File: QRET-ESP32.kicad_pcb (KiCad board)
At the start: 2 copper layers, 9 parts, among them J1 Conn_01x04_Socket, J2 Conn_01x02_Socket, J3 Conn_01x02_Socket, J4 Conn_02x04_Counter_Clockwise, J5 Conn_01x02_Socket, J6 Conn_01x02_Socket, J7 Conn_01x02_Socket, U1 ESP32-S2-DevKitC-1, U2 ADS1115IDGS

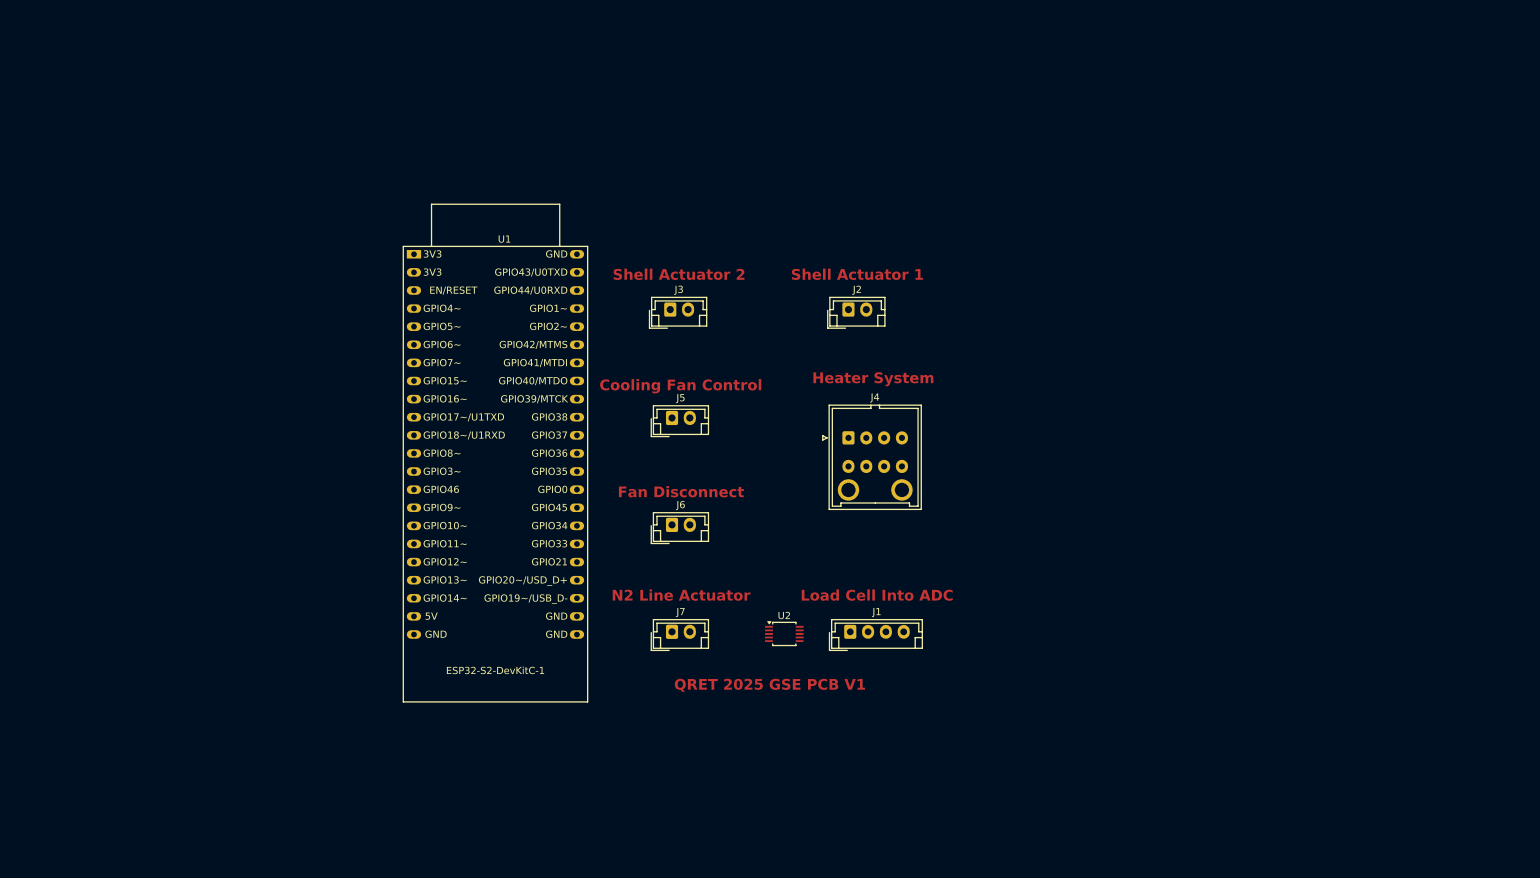
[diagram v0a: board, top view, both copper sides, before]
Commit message: Updated to 4-pin fans, moved power pages together, deleted old reference.
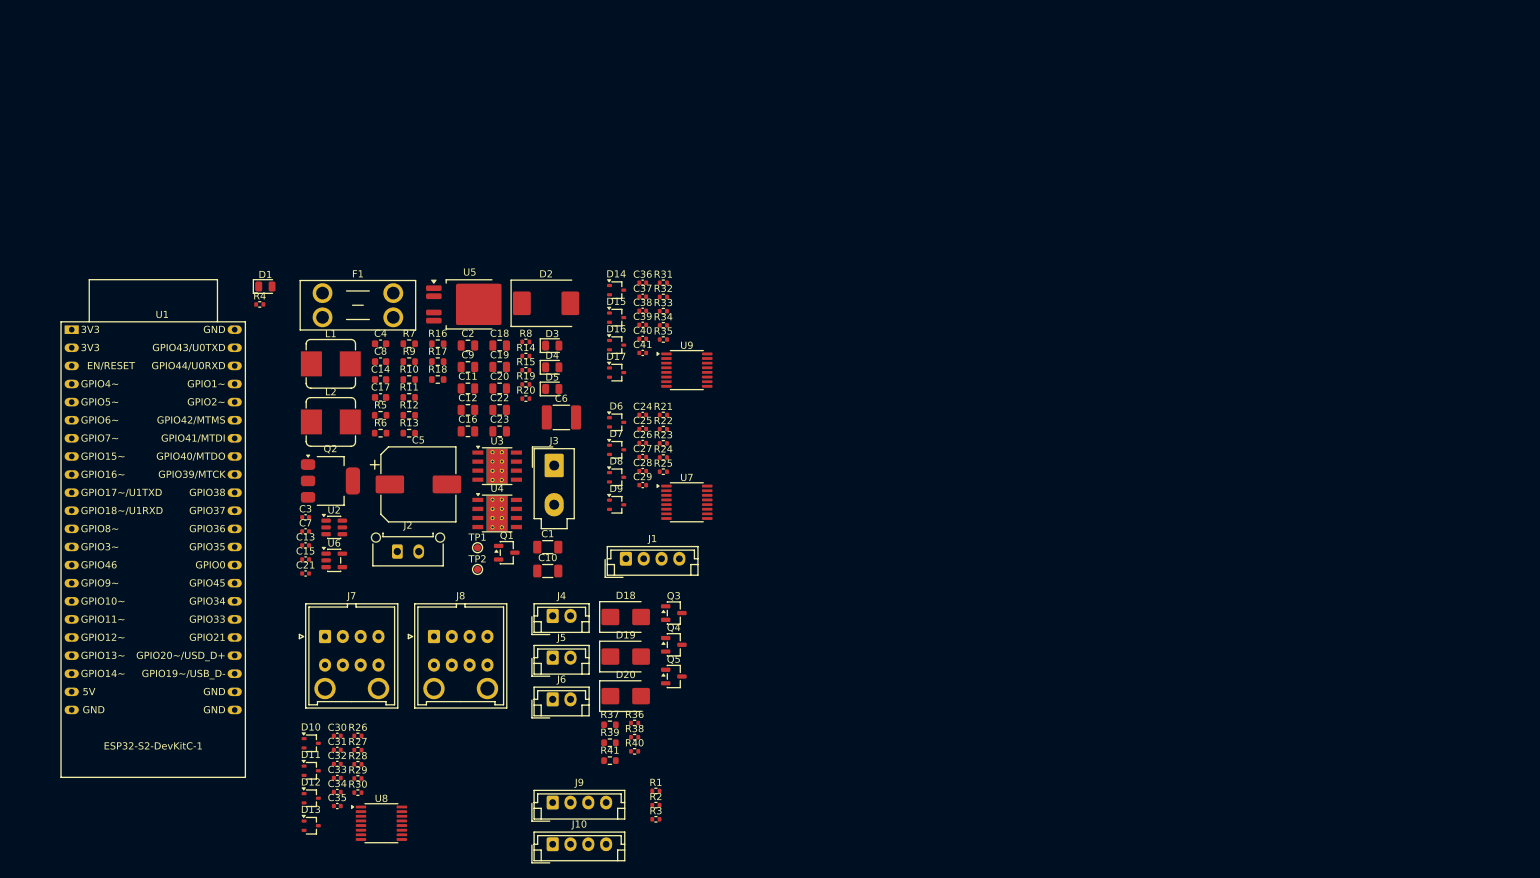
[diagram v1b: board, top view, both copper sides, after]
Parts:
- added C1: 10uF, Capacitor_SMD:C_1206_3216Metric, F.Cu at (140.8, 110.3)
- added C10: 10uF, Capacitor_SMD:C_1206_3216Metric, F.Cu at (140.8, 113.7)
- added C11: 22uF, Capacitor_SMD:C_0805_2012Metric, F.Cu at (129.6, 88.1)
- added C12: 220nF, Capacitor_SMD:C_0805_2012Metric, F.Cu at (129.6, 91.1)
- added C13: 0.1μF, Capacitor_SMD:C_0402_1005Metric, F.Cu at (106.8, 110.1)
- added C14: 1uF, Capacitor_SMD:C_0603_1608Metric, F.Cu at (117.4, 86.8)
- added C15: 0.1μF, Capacitor_SMD:C_0402_1005Metric, F.Cu at (106.8, 112.0)
- added C16: 10uF, Capacitor_SMD:C_0805_2012Metric, F.Cu at (129.6, 94.1)
- added C17: 3pF, Capacitor_SMD:C_0603_1608Metric, F.Cu at (117.4, 89.3)
- added C18: 22uF, Capacitor_SMD:C_0805_2012Metric, F.Cu at (134.1, 82.0)
- added C19: 22uF, Capacitor_SMD:C_0805_2012Metric, F.Cu at (134.1, 85.0)
- added C2: 220nF, Capacitor_SMD:C_0805_2012Metric, F.Cu at (129.6, 82.0)
- added C20: 10uF, Capacitor_SMD:C_0805_2012Metric, F.Cu at (134.1, 88.1)
- added C21: 0.1μF, Capacitor_SMD:C_0402_1005Metric, F.Cu at (106.8, 114.0)
- added C22: 10uF, Capacitor_SMD:C_0805_2012Metric, F.Cu at (134.1, 91.1)
- added C23: 10uF, Capacitor_SMD:C_0805_2012Metric, F.Cu at (134.1, 94.1)
- added C24: 0.1μF, Capacitor_SMD:C_0402_1005Metric, F.Cu at (154.1, 91.8)
- added C25: 0.1μF, Capacitor_SMD:C_0402_1005Metric, F.Cu at (154.1, 93.7)
- added C26: 150nF, Capacitor_SMD:C_0402_1005Metric, F.Cu at (154.1, 95.7)
- added C27: 150nF, Capacitor_SMD:C_0402_1005Metric, F.Cu at (154.1, 97.7)
- added C28: 150nF, Capacitor_SMD:C_0402_1005Metric, F.Cu at (154.1, 99.7)
- added C29: 150nF, Capacitor_SMD:C_0402_1005Metric, F.Cu at (154.1, 101.6)
- added C3: 0.1μF, Capacitor_SMD:C_0402_1005Metric, F.Cu at (106.8, 106.1)
- added C30: 0.1μF, Capacitor_SMD:C_0402_1005Metric, F.Cu at (111.3, 136.8)
- added C31: 0.1μF, Capacitor_SMD:C_0402_1005Metric, F.Cu at (111.3, 138.8)
- added C32: 150nF, Capacitor_SMD:C_0402_1005Metric, F.Cu at (111.3, 140.7)
- added C33: 150nF, Capacitor_SMD:C_0402_1005Metric, F.Cu at (111.3, 142.7)
- added C34: 150nF, Capacitor_SMD:C_0402_1005Metric, F.Cu at (111.3, 144.7)
- added C35: 150nF, Capacitor_SMD:C_0402_1005Metric, F.Cu at (111.3, 146.6)
- added C36: 0.1μF, Capacitor_SMD:C_0402_1005Metric, F.Cu at (154.1, 73.2)
- added C37: 0.1μF, Capacitor_SMD:C_0402_1005Metric, F.Cu at (154.1, 75.2)
- added C38: 150nF, Capacitor_SMD:C_0402_1005Metric, F.Cu at (154.1, 77.2)
- added C39: 150nF, Capacitor_SMD:C_0402_1005Metric, F.Cu at (154.1, 79.1)
- added C4: 1uF, Capacitor_SMD:C_0603_1608Metric, F.Cu at (117.4, 81.8)
- added C40: 150nF, Capacitor_SMD:C_0402_1005Metric, F.Cu at (154.1, 81.1)
- added C41: 150nF, Capacitor_SMD:C_0402_1005Metric, F.Cu at (154.1, 83.1)
- added C5: 100uF, Capacitor_SMD:CP_Elec_10x10, F.Cu at (122.7, 101.5)
- added C6: 10uF, Capacitor_SMD:C_1812_4532Metric, F.Cu at (142.7, 92.1)
- added C7: 0.1μF, Capacitor_SMD:C_0402_1005Metric, F.Cu at (106.8, 108.1)
- added C8: 3pF, Capacitor_SMD:C_0603_1608Metric, F.Cu at (117.4, 84.3)
- added C9: 22uF, Capacitor_SMD:C_0805_2012Metric, F.Cu at (129.6, 85.0)
- added D1: LED-Y, LED_SMD:LED_0805_2012Metric, F.Cu at (101.2, 73.8)
- added D10: BAT54SW, Package_TO_SOT_SMD:SOT-323_SC-70, F.Cu at (107.6, 137.8)
- added D11: BAT54SW, Package_TO_SOT_SMD:SOT-323_SC-70, F.Cu at (107.6, 141.7)
- added D12: BAT54SW, Package_TO_SOT_SMD:SOT-323_SC-70, F.Cu at (107.6, 145.5)
- added D13: BAT54SW, Package_TO_SOT_SMD:SOT-323_SC-70, F.Cu at (107.6, 149.4)
- added D14: BAT54SW, Package_TO_SOT_SMD:SOT-323_SC-70, F.Cu at (150.5, 74.3)
- added D15: BAT54SW, Package_TO_SOT_SMD:SOT-323_SC-70, F.Cu at (150.5, 78.1)
- added D16: BAT54SW, Package_TO_SOT_SMD:SOT-323_SC-70, F.Cu at (150.5, 82.0)
- added D17: BAT54SW, Package_TO_SOT_SMD:SOT-323_SC-70, F.Cu at (150.5, 85.8)
- added D18: SK44BL, Diode_SMD:D_SMB, F.Cu at (151.8, 120.1)
- added D19: SK44BL, Diode_SMD:D_SMB, F.Cu at (151.8, 125.7)
- added D2: SMCJ26A-13-F, Diode_SMD:D_SMC, F.Cu at (140.6, 76.1)
- added D20: SK44BL, Diode_SMD:D_SMB, F.Cu at (151.8, 131.2)
- added D3: LED-G, LED_SMD:LED_0805_2012Metric, F.Cu at (141.4, 82.1)
- added D4: LED-G, LED_SMD:LED_0805_2012Metric, F.Cu at (141.4, 85.1)
- added D5: LED-G, LED_SMD:LED_0805_2012Metric, F.Cu at (141.4, 88.1)
- added D6: BAT54SW, Package_TO_SOT_SMD:SOT-323_SC-70, F.Cu at (150.5, 92.8)
- added D7: BAT54SW, Package_TO_SOT_SMD:SOT-323_SC-70, F.Cu at (150.5, 96.7)
- added D8: BAT54SW, Package_TO_SOT_SMD:SOT-323_SC-70, F.Cu at (150.5, 100.5)
- added D9: BAT54SW, Package_TO_SOT_SMD:SOT-323_SC-70, F.Cu at (150.5, 104.4)
- added F1: Fuse, Fuse:Fuseholder_Blade_Mini_Keystone_3568, F.Cu at (109.2, 74.7)
- added J10: Conn_01x04, Connector_JST:JST_EH_B4B-EH-A_1x04_P2.50mm_Vertical, F.Cu at (141.5, 152.0)
- added J8: Conn_02x04_Counter_Clockwise, Connector_JST:JST_J2100_B08B-J21DK-GGXR_2x04_P2.50x4.00mm_Vertical, F.Cu at (124.9, 122.9)
- added J9: Conn_01x04, Connector_JST:JST_EH_B4B-EH-A_1x04_P2.50mm_Vertical, F.Cu at (141.5, 146.2)
- added L1: 16uH, Inductor_SMD:L_Bourns_SRP7028A_7.3x6.6mm, F.Cu at (110.4, 84.6)
- added L2: 4.7uH, Inductor_SMD:L_Bourns_SRP7028A_7.3x6.6mm, F.Cu at (110.4, 92.8)
- added Q1: BSS138, Package_TO_SOT_SMD:SOT-23-3, F.Cu at (135.1, 111.1)
- added Q2: DMP6023LE-13, Package_TO_SOT_SMD:SOT-223-3_TabPin2, F.Cu at (110.3, 101.0)
- added Q3: BSS138, Package_TO_SOT_SMD:SOT-23-3, F.Cu at (158.5, 119.6)
- added Q4: BSS138, Package_TO_SOT_SMD:SOT-23-3, F.Cu at (158.5, 124.0)
- added Q5: BSS138, Package_TO_SOT_SMD:SOT-23-3, F.Cu at (158.5, 128.5)
- added R1: 3.3k, Resistor_SMD:R_0402_1005Metric, F.Cu at (156.0, 144.5)
- added R10: 100k, Resistor_SMD:R_0603_1608Metric, F.Cu at (121.4, 86.8)
- added R11: 100k, Resistor_SMD:R_0603_1608Metric, F.Cu at (121.4, 89.3)
- added R12: 9.09k, Resistor_SMD:R_0603_1608Metric, F.Cu at (121.4, 91.8)
- added R13: 470k, Resistor_SMD:R_0603_1608Metric, F.Cu at (121.4, 94.3)
- added R14: 10k, Resistor_SMD:R_0402_1005Metric, F.Cu at (137.8, 83.5)
- added R15: 10k, Resistor_SMD:R_0402_1005Metric, F.Cu at (137.8, 85.5)
- added R16: 100k, Resistor_SMD:R_0603_1608Metric, F.Cu at (125.4, 81.8)
- added R17: 100k, Resistor_SMD:R_0603_1608Metric, F.Cu at (125.4, 84.3)
- added R18: 23.2k, Resistor_SMD:R_0603_1608Metric, F.Cu at (125.4, 86.8)
- added R19: 1.2k, Resistor_SMD:R_0402_1005Metric, F.Cu at (137.8, 87.5)
- added R2: 3.3k, Resistor_SMD:R_0402_1005Metric, F.Cu at (156.0, 146.5)
- added R20: 3.3k, Resistor_SMD:R_0402_1005Metric, F.Cu at (137.8, 89.5)
- added R21: 1k, Resistor_SMD:R_0402_1005Metric, F.Cu at (157.0, 91.8)
- added R22: 1k, Resistor_SMD:R_0402_1005Metric, F.Cu at (157.0, 93.8)
- added R23: 1k, Resistor_SMD:R_0402_1005Metric, F.Cu at (157.0, 95.8)
- added R24: 1k, Resistor_SMD:R_0402_1005Metric, F.Cu at (157.0, 97.8)
- added R25: 10k, Resistor_SMD:R_0402_1005Metric, F.Cu at (157.0, 99.7)
- added R26: 1k, Resistor_SMD:R_0402_1005Metric, F.Cu at (114.2, 136.8)
- added R27: 1k, Resistor_SMD:R_0402_1005Metric, F.Cu at (114.2, 138.8)
- added R28: 1k, Resistor_SMD:R_0402_1005Metric, F.Cu at (114.2, 140.8)
- added R29: 1k, Resistor_SMD:R_0402_1005Metric, F.Cu at (114.2, 142.8)
- added R3: 3.3k, Resistor_SMD:R_0402_1005Metric, F.Cu at (156.0, 148.5)
- added R30: 10k, Resistor_SMD:R_0402_1005Metric, F.Cu at (114.2, 144.8)
- added R31: 1k, Resistor_SMD:R_0402_1005Metric, F.Cu at (157.0, 73.2)
- added R32: 1k, Resistor_SMD:R_0402_1005Metric, F.Cu at (157.0, 75.2)
- added R33: 1k, Resistor_SMD:R_0402_1005Metric, F.Cu at (157.0, 77.2)
- added R34: 1k, Resistor_SMD:R_0402_1005Metric, F.Cu at (157.0, 79.2)
- added R35: 10k, Resistor_SMD:R_0402_1005Metric, F.Cu at (157.0, 81.2)
- added R36: 100, Resistor_SMD:R_0402_1005Metric, F.Cu at (153.0, 135.0)
- added R37: 100k, Resistor_SMD:R_0603_1608Metric, F.Cu at (149.5, 135.2)
- added R38: 100, Resistor_SMD:R_0402_1005Metric, F.Cu at (153.0, 137.0)
- added R39: 100k, Resistor_SMD:R_0603_1608Metric, F.Cu at (149.5, 137.8)
- added R4: 1k, Resistor_SMD:R_0402_1005Metric, F.Cu at (100.4, 76.3)
- added R40: 100, Resistor_SMD:R_0402_1005Metric, F.Cu at (153.0, 139.0)
- added R41: 100k, Resistor_SMD:R_0603_1608Metric, F.Cu at (149.5, 140.3)
- added R5: 100k, Resistor_SMD:R_0603_1608Metric, F.Cu at (117.4, 91.8)
- added R6: 100k, Resistor_SMD:R_0603_1608Metric, F.Cu at (117.4, 94.3)
- added R7: 100k, Resistor_SMD:R_0603_1608Metric, F.Cu at (121.4, 81.8)
- added R8: 39k, Resistor_SMD:R_0402_1005Metric, F.Cu at (137.8, 81.5)
- added R9: 100k, Resistor_SMD:R_0603_1608Metric, F.Cu at (121.4, 84.3)
- added TP1: TP_+3.3V, TestPoint:TestPoint_Pad_D1.0mm, F.Cu at (131.0, 110.4)
- added TP2: TP_+5V, TestPoint:TestPoint_Pad_D1.0mm, F.Cu at (131.0, 113.5)
- added U3: LMR33630BDDA, Package_SO:Texas_HSOP-8-1EP_3.9x4.9mm_P1.27mm_ThermalVias, F.Cu at (133.7, 99.0)
- added U4: LMR33630BDDA, Package_SO:Texas_HSOP-8-1EP_3.9x4.9mm_P1.27mm_ThermalVias, F.Cu at (133.7, 105.6)
- added U5: TPS78533QKVURQ1, Package_TO_SOT_SMD:TO-252-4, F.Cu at (129.9, 76.3)
- added U6: TPS78450QDBVRQ1, Package_TO_SOT_SMD:SOT-23-5, F.Cu at (110.9, 112.2)
- added U7: ADS112C04, Package_SO:TSSOP-16_4.4x5mm_P0.65mm, F.Cu at (160.3, 104.0)
- added U8: ADS112C04, Package_SO:TSSOP-16_4.4x5mm_P0.65mm, F.Cu at (117.5, 149.1)
- added U9: ADS112C04, Package_SO:TSSOP-16_4.4x5mm_P0.65mm, F.Cu at (160.3, 85.5)
- J1: value Conn_01x04_Socket -> Conn_01x04
- J2: value Conn_01x02_Socket -> Conn_01x02; footprint Connector_JST:JST_EH_B2B-EH-A_1x02_P2.50mm_Vertical -> Connector_Molex:Molex_Micro-Fit_3.0_43650-0215_1x02_P3.00mm_Vertical
- J3: value Conn_01x02_Socket -> Conn_02x01; footprint Connector_JST:JST_EH_B2B-EH-A_1x02_P2.50mm_Vertical -> Connector_Molex:Molex_Mini-Fit_Jr_5566-02A_2x01_P4.20mm_Vertical
- J4: value Conn_02x04_Counter_Clockwise -> Conn_01x02; footprint Connector_JST:JST_J2100_B08B-J21DK-GGXR_2x04_P2.50x4.00mm_Vertical -> Connector_JST:JST_EH_B2B-EH-A_1x02_P2.50mm_Vertical
- J5, J6: value Conn_01x02_Socket -> Conn_01x02
- J7: value Conn_01x02_Socket -> Conn_02x04_Counter_Clockwise; footprint Connector_JST:JST_EH_B2B-EH-A_1x02_P2.50mm_Vertical -> Connector_JST:JST_J2100_B08B-J21DK-GGXR_2x04_P2.50x4.00mm_Vertical
- U2: value ADS1115IDGS -> LM3880-1AA; footprint Package_SO:TSSOP-10_3x3mm_P0.5mm -> Package_TO_SOT_SMD:SOT-23-6
- moved J2 71.8 mm to (119.7, 110.9)
- moved U2 64.9 mm to (110.9, 107.6)
- moved U1 49.2 mm to (74.0, 79.8)
- moved J7 48.7 mm to (109.6, 122.9)
- moved J4 48.4 mm to (141.5, 120.0)
- moved J5 37.6 mm to (141.5, 125.8)
- moved J1 33.1 mm to (151.8, 112.0)
- moved J6 29.6 mm to (141.5, 131.7)
- moved J3 27.3 mm to (141.7, 98.9)
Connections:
- J1 pad 1: Net-(J1-Pin_1) -> /Load_Cell/5V_In
- J1 pad 2: Net-(J1-Pin_2) -> Load_Cell+
- J1 pad 3: Net-(J1-Pin_3) -> Load_Cell-
- J1 pad 4: Net-(J1-Pin_4) -> GND
- J2 pad 2: Net-(J1-Pin_4) -> /Power_Regulation/PWR_SQ
- J3 pad 2: Net-(J1-Pin_4) -> GND
- J4 pad 1: Net-(J4-Pin_1) -> +24V
- J4 pad 2: Net-(J4-Pin_2) -> Net-(D18-A)
- J5 pad 1: Net-(J5-Pin_1) -> +24V
- J5 pad 2: Net-(J1-Pin_4) -> Net-(D19-A)
- J6 pad 1: Net-(J6-Pin_1) -> +24V
- J6 pad 2: Net-(J1-Pin_4) -> Net-(D20-A)
- J7 pad 1: Net-(J7-Pin_1) -> Heat_1_Power
- J7 pad 2: Net-(J4-Pin_7) -> Heat_1_Variable
- U1 pad 1: Net-(U2-VDD) -> unconnected-(U1-3V3-Pad1)
- U1 pad 12: Net-(J4-Pin_5) -> unconnected-(U1-GPIO8/ADC1_CH7-Pad12)
- U1 pad 13: Net-(J4-Pin_6) -> unconnected-(U1-GPIO3/ADC1_CH2-Pad13)
- U1 pad 21: Net-(J7-Pin_1) -> unconnected-(U1-5V-Pad21)
- U1 pad 22: Net-(J4-Pin_7) -> unconnected-(U1-GND-Pad22)
- U1 pad 24: Net-(J1-Pin_4) -> unconnected-(U1-GND-Pad24)
- U1 pad 27: Net-(J2-Pin_1) -> /ESP32-Breakout/WIFI_IND
- U1 pad 28: Net-(J3-Pin_1) -> I2C_Clock
- U1 pad 29: Net-(J6-Pin_1) -> I2C_Data
- U1 pad 30: Net-(J5-Pin_1) -> Nitrous_Control
- U1 pad 31: unconnected-(U1-GPIO0-Pad31) -> A2_Control
- U1 pad 32: unconnected-(U1-GPIO35-Pad32) -> A1_Control
- U1 pad 33: unconnected-(U1-GPIO36-Pad33) -> Fan_2_PWM
- U1 pad 34: Net-(J1-Pin_3) -> Fan_1_PWM
- U1 pad 35: Net-(U1-GPIO38) -> Heat_2_Power
- U1 pad 36: unconnected-(U1-GPIO39/MTCK-Pad36) -> Heat_1_Power
- U1 pad 37: unconnected-(U1-GPIO40/MTDO-Pad37) -> DRDY3
- U1 pad 38: unconnected-(U1-GPIO41/MTDI-Pad38) -> DRDY2
- U1 pad 39: unconnected-(U1-GPIO42/MTMS-Pad39) -> DRDY1
- U1 pad 4: Net-(J4-Pin_1) -> unconnected-(U1-GPIO4/ADC1_CH3-Pad4)
- U1 pad 40: unconnected-(U1-GPIO2/ADC1_CH1-Pad40) -> Fan_2_Control
- U1 pad 41: unconnected-(U1-GPIO1/ADC1_CH0-Pad41) -> Fan_1_Control
- U1 pad 5: Net-(J4-Pin_2) -> unconnected-(U1-GPIO5/ADC1_CH4-Pad5)
- U1 pad 6: Net-(J4-Pin_3) -> unconnected-(U1-GPIO6/ADC1_CH5-Pad6)
- U1 pad 7: Net-(J4-Pin_4) -> unconnected-(U1-GPIO7/ADC1_CH6-Pad7)
- U2 pad 1: unconnected-(U2-ADDR-Pad1) -> /Power_Regulation/PWR_SQ
- U2 pad 2: unconnected-(U2-ALERT/RDY-Pad2) -> GND
- U2 pad 3: Net-(J1-Pin_4) -> Net-(J2-Pin_1)
- U2 pad 4: Net-(J1-Pin_1) -> Net-(Q1-G)
- U2 pad 5: Net-(J1-Pin_2) -> /Power_Regulation/+5V_EN
- U2 pad 6: unconnected-(U2-AIN2-Pad6) -> /Power_Regulation/+3.3V_EN
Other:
- board text removed: "Cooling Fan Control"
- board text removed: "Fan Disconnect"
- board text removed: "Heater System"
- board text removed: "Load Cell Into ADC"
- board text removed: "N2 Line Actuator"
- board text removed: "QRET 2025 GSE PCB V1"
- board text removed: "Shell Actuator 1"
- board text removed: "Shell Actuator 2"

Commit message: Started placement of ADC1 and 2.
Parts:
- moved D13 132.0 mm to (195.2, 50.7), turned to 90 degrees
- moved D11 129.4 mm to (195.2, 46.4), turned to 90 degrees
- moved C35 128.8 mm to (197.6, 51.0), turned to -90 degrees
- moved R29 128.6 mm to (200.6, 47.5), turned to 180 degrees
- moved C33 128.5 mm to (197.6, 47.5), turned to -90 degrees
- moved D12 126.0 mm to (195.2, 55.0), turned to 90 degrees
- moved C34 124.7 mm to (197.6, 54.6), turned to -90 degrees
- moved R28 124.6 mm to (200.6, 51.0), turned to 180 degrees
- moved J7 121.8 mm to (207.2, 50.0)
- moved C31 120.8 mm to (189.7, 46.9), turned to 90 degrees
- moved R27 120.6 mm to (200.6, 54.6), turned to 180 degrees
- moved U8 120.1 mm to (189.4, 52.9), turned to 90 degrees
- moved C32 119.4 mm to (197.6, 58.2), turned to -90 degrees
- moved D10 117.6 mm to (195.2, 59.3), turned to 90 degrees
- moved R26 116.8 mm to (200.6, 58.1), turned to 180 degrees
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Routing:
- net Heat_1_TB: track 0.00 -> 16.8 mm, vias 0 -> 2
- net Heat_1_TA: track 0.00 -> 13.6 mm
- net Heat_1_Variable: track 0.00 -> 11.1 mm
- net Heat_1_TC: track 0.00 -> 7.85 mm
- net Heat_1_Power: track 0.00 -> 3.16 mm, vias 0 -> 2
- net /ADC2/AIN1: track 0.00 -> 2.64 mm
- net /ADC2/AIN3: track 0.00 -> 2.63 mm

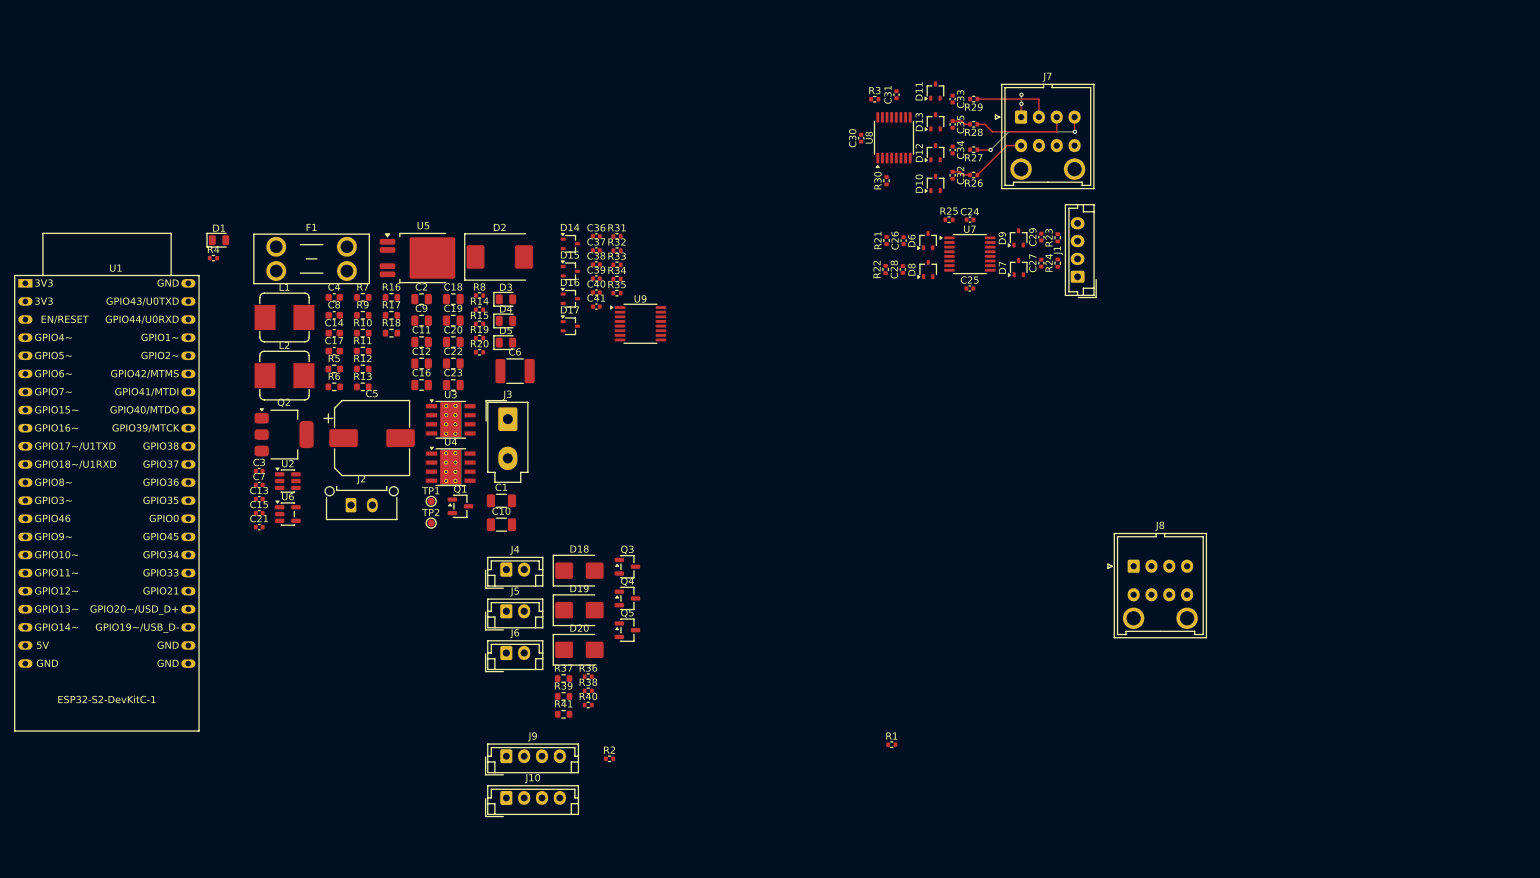
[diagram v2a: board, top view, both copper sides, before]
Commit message: Adopted 4-layer setup and organized placement
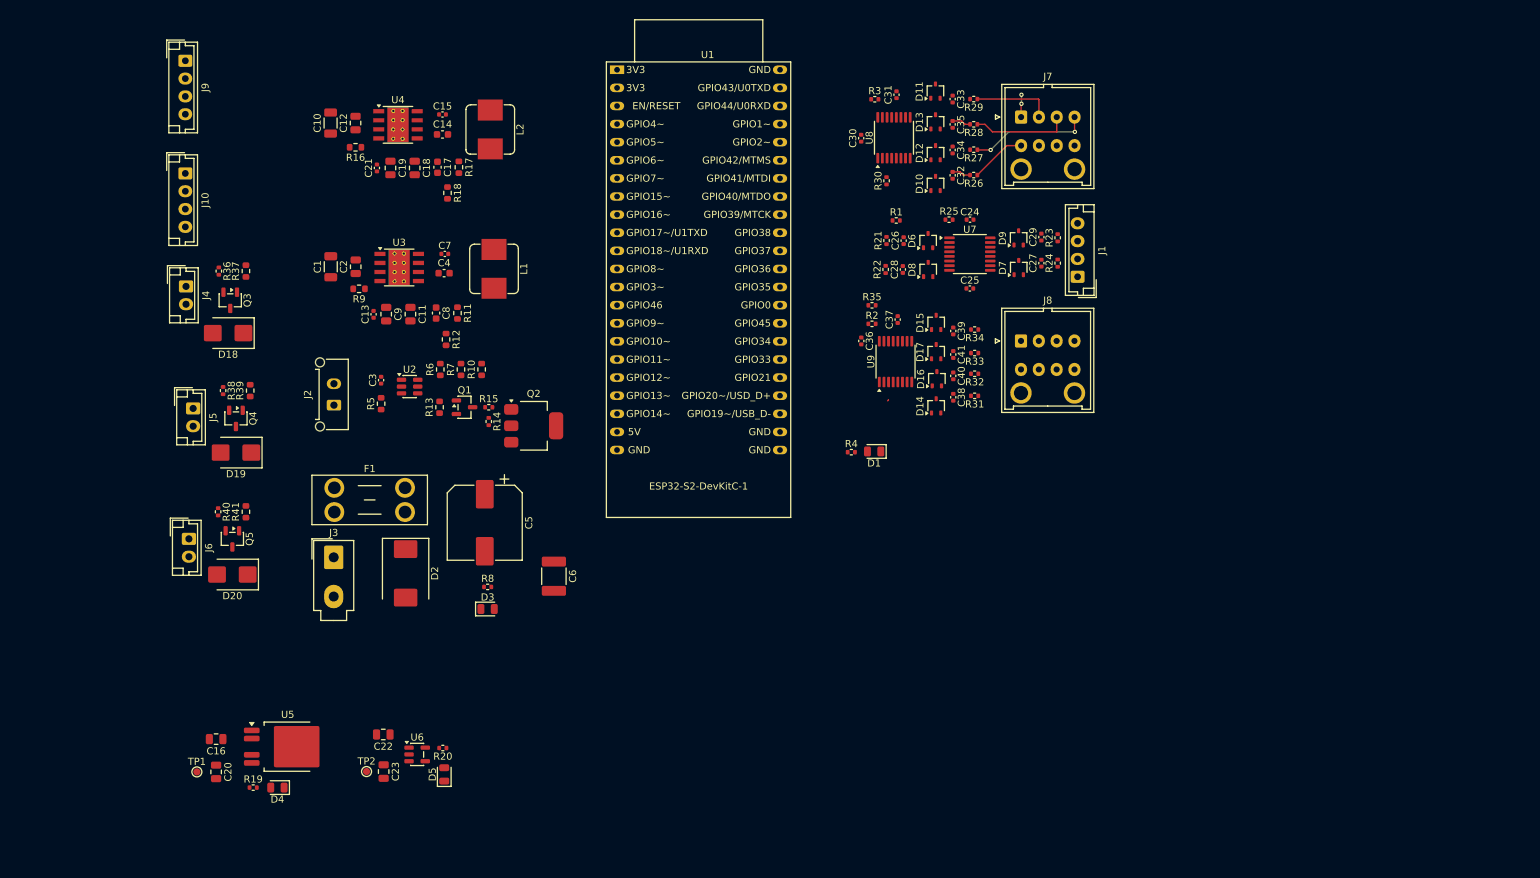
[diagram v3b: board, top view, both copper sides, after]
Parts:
- moved J9 107.4 mm to (90.0, 42.1), turned to -90 degrees
- moved J10 98.5 mm to (90.0, 57.9), turned to -90 degrees
- moved D1 96.6 mm to (186.6, 96.9), turned to 180 degrees
- moved R4 93.5 mm to (183.4, 97.0)
- moved U1 88.2 mm to (150.5, 43.4)
- moved R36 77.0 mm to (94.7, 71.6), turned to -90 degrees
- moved R1 73.5 mm to (189.7, 64.5)
- moved D4 72.9 mm to (102.9, 144.1), turned to 180 degrees
- moved R37 72.5 mm to (98.5, 71.6), turned to 90 degrees
- moved R2 71.3 mm to (186.3, 79.0)
- moved U5 71.1 mm to (104.3, 138.3)
- moved R19 70.6 mm to (99.5, 144.1)
- moved C20 68.9 mm to (94.3, 141.8), turned to -90 degrees
- moved Q3 67.1 mm to (96.3, 75.7), turned to -90 degrees
- moved R38 66.3 mm to (95.3, 88.4), turned to -90 degrees
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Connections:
- C14 pad 1: /Power_Regulation/VCC -> /Power_Regulation/VCC-5
- C15 pad 2: /Power_Regulation/SW -> /Power_Regulation/SW-5
- C4 pad 1: /Power_Regulation/VCC -> /Power_Regulation/VCC-12
- C7 pad 2: /Power_Regulation/SW -> /Power_Regulation/SW-12
- L1 pad 1: /Power_Regulation/SW -> /Power_Regulation/SW-12
- L2 pad 1: /Power_Regulation/SW -> /Power_Regulation/SW-5
- R16 pad 1: /Power_Regulation/24_POWER_GOOD -> 24V_GOOD
- R9 pad 1: /Power_Regulation/12_POWER_GOOD -> 12V_GOOD
- U1 pad 15: unconnected-(U1-GPIO9/ADC1_CH8-Pad15) -> 24V_GOOD
- U1 pad 16: unconnected-(U1-GPIO10/ADC1_CH9-Pad16) -> 12V_GOOD
- U3 pad 4: /Power_Regulation/12_POWER_GOOD -> 12V_GOOD
- U3 pad 6: /Power_Regulation/VCC -> /Power_Regulation/VCC-12
- U3 pad 8: /Power_Regulation/SW -> /Power_Regulation/SW-12
- U4 pad 4: /Power_Regulation/24_POWER_GOOD -> 24V_GOOD
- U4 pad 6: /Power_Regulation/VCC -> /Power_Regulation/VCC-5
- U4 pad 8: /Power_Regulation/SW -> /Power_Regulation/SW-5
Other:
- copper layers 2 -> 4
